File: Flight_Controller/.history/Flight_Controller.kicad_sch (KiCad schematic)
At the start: 0 parts

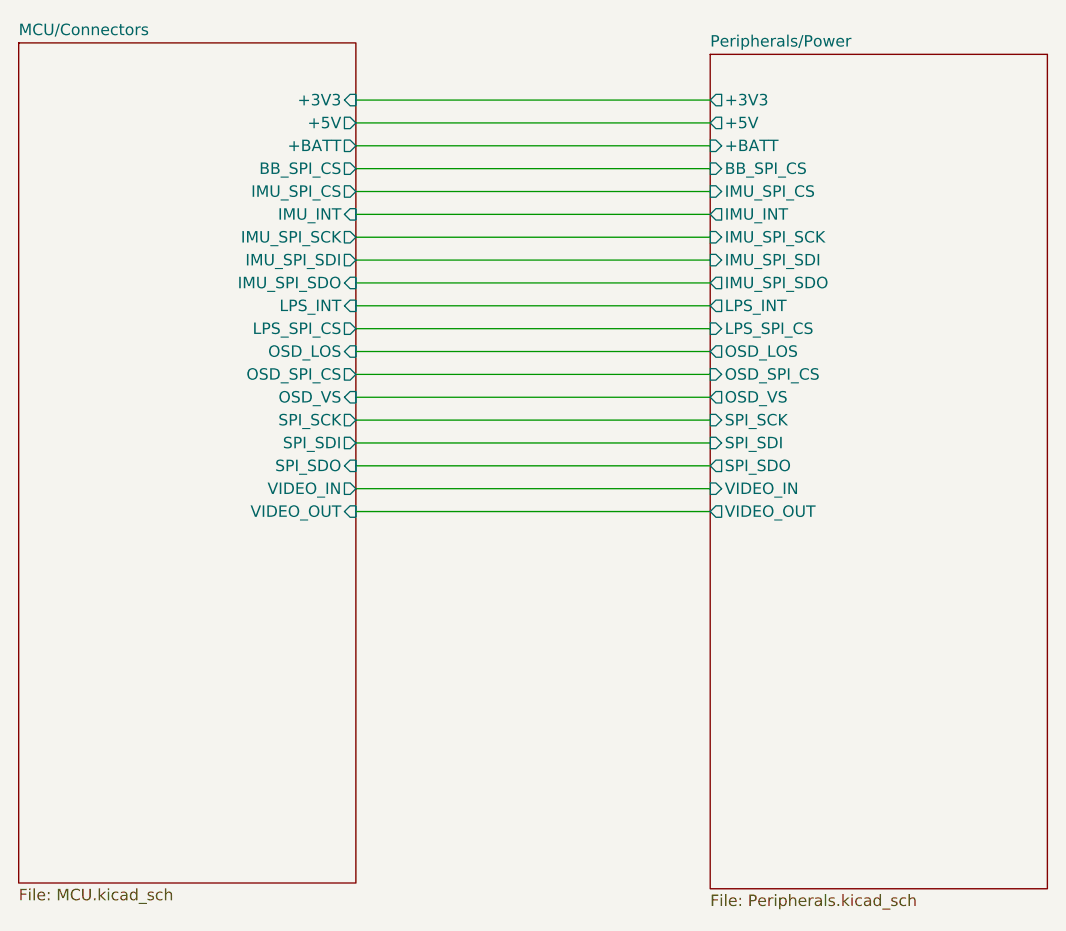
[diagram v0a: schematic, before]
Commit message: Connected all new parts to MCU, added support for hexcopter
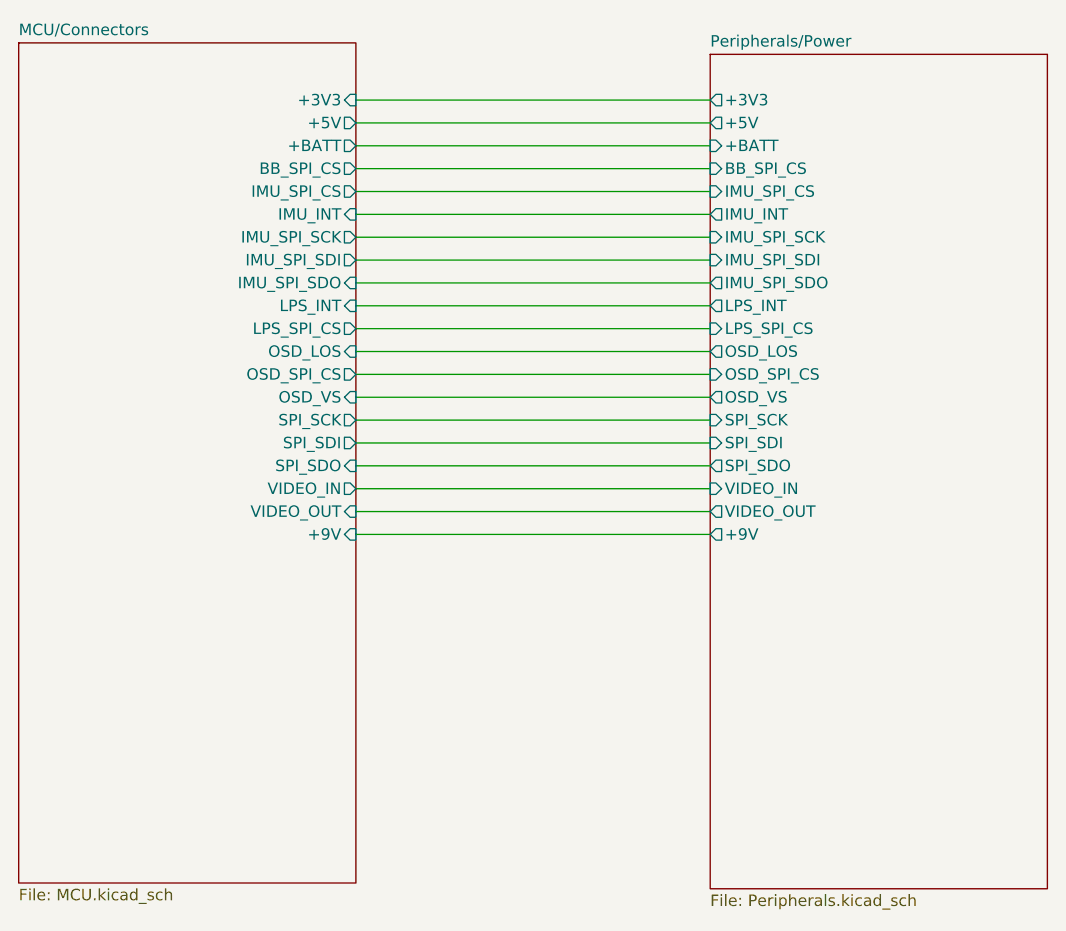
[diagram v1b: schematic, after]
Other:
- sheet MCU/Connectors ports: added +9V; removed none
- sheet Peripherals/Power ports: added +9V; removed none
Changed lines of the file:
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@@
 	(wire
 		(pts
+			(xy 54.61 153.67) (xy 93.98 153.67)
+		)
+		(stroke
+			(width 0)
+			(type default)
+		)
+	)
+	(wire
+		(pts
 			(xy 54.61 143.51) (xy 93.98 143.51)
 		)
@@
 			)
 		)
+		(pin "+9V" input
+			(at 54.61 153.67 0)
+			(effects
+				(font
+					(size 1.27 1.27)
+				)
+				(justify right)
+			)
+		)
 		(instances
 			(project "Flight_Controller"
@@
 			(effects
 				(font
+					(size 1.27 1.27)
+				)
+				(justify left)
+			)
+		)
+		(pin "+9V" output
+			(at 93.98 153.67 180)
+			(effects
+				(font

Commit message: Routing Done!
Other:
- sheet MCU/Connectors ports: added I2C_SCL1, I2C_SDA1, OSD_SPI_SCK, OSD_SPI_SDI, OSD_SPI_SDO; removed LPS_SPI_CS, OSD_LOS, OSD_VS
- sheet Peripherals/Power ports: added I2C_SCL1, I2C_SDA1, OSD_SPI_SCK, OSD_SPI_SDI, OSD_SPI_SDO; removed LPS_SPI_CS, OSD_LOS, OSD_VS
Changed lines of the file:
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@@
 	(wire
 		(pts
-			(xy 54.61 120.65) (xy 93.98 120.65)
+			(xy 54.61 153.67) (xy 93.98 153.67)
 		)
 		(stroke
@@
 	(wire
 		(pts
-			(xy 54.61 151.13) (xy 93.98 151.13)
+			(xy 54.61 120.65) (xy 93.98 120.65)
 		)
 		(stroke
@@
 	(wire
 		(pts
-			(xy 54.61 146.05) (xy 93.98 146.05)
+			(xy 54.61 143.51) (xy 93.98 143.51)
 		)
 		(stroke
@@
 	(wire
 		(pts
-			(xy 54.61 130.81) (xy 93.98 130.81)
+			(xy 54.61 138.43) (xy 93.98 138.43)
 		)
 		(stroke
@@
 	(wire
 		(pts
-			(xy 54.61 138.43) (xy 93.98 138.43)
+			(xy 54.61 140.97) (xy 93.98 140.97)
 		)
 		(stroke
@@
 	(wire
 		(pts
-			(xy 54.61 153.67) (xy 93.98 153.67)
+			(xy 54.61 146.05) (xy 93.98 146.05)
 		)
 		(stroke
@@
 	(wire
 		(pts
-			(xy 54.61 143.51) (xy 93.98 143.51)
+			(xy 54.61 135.89) (xy 93.98 135.89)
 		)
 		(stroke
@@
 	(wire
 		(pts
+			(xy 54.61 156.21) (xy 93.98 156.21)
+		)
+		(stroke
+			(width 0)
+			(type default)
+		)
+	)
+	(wire
+		(pts
 			(xy 54.61 133.35) (xy 93.98 133.35)
 		)
@@
 	(wire
 		(pts
-			(xy 54.61 140.97) (xy 93.98 140.97)
+			(xy 54.61 158.75) (xy 93.98 158.75)
 		)
 		(stroke
@@
 	(wire
 		(pts
+			(xy 54.61 151.13) (xy 93.98 151.13)
+		)
+		(stroke
+			(width 0)
+			(type default)
+		)
+	)
+	(wire
+		(pts
 			(xy 54.61 123.19) (xy 93.98 123.19)
 		)
@@
 	(wire
 		(pts
-			(xy 54.61 135.89) (xy 93.98 135.89)
+			(xy 54.61 130.81) (xy 93.98 130.81)
 		)
 		(stroke
@@
 			)
 		)
-		(pin "LPS_SPI_CS" output
+		(pin "OSD_SPI_CS" output
 			(at 54.61 130.81 0)
 			(effects
@@
 			)
 		)
-		(pin "OSD_LOS" input
+		(pin "SPI_SCK" output
 			(at 54.61 133.35 0)
 			(effects
@@
 			)
 		)
-		(pin "OSD_SPI_CS" output
+		(pin "SPI_SDI" output
 			(at 54.61 135.89 0)
 			(effects
@@
 			)
 		)
-		(pin "OSD_VS" input
+		(pin "SPI_SDO" input
 			(at 54.61 138.43 0)
 			(effects
@@
 			)
 		)
-		(pin "SPI_SCK" output
+		(pin "VIDEO_IN" output
 			(at 54.61 140.97 0)
 			(effects
@@
 			)
 		)
-		(pin "SPI_SDI" output
+		(pin "VIDEO_OUT" input
 			(at 54.61 143.51 0)
 			(effects
@@
 			)
 		)
-		(pin "SPI_SDO" input
+		(pin "+9V" input
 			(at 54.61 146.05 0)
 			(effects
@@
 			)
 		)
-		(pin "VIDEO_IN" output
+		(pin "I2C_SCL1" output
 			(at 54.61 148.59 0)
 			(effects
@@
 			)
 		)
-		(pin "VIDEO_OUT" input
+		(pin "I2C_SDA1" bidirectional
 			(at 54.61 151.13 0)
 			(effects
@@
 			)
 		)
-		(pin "+9V" input
+		(pin "OSD_SPI_SCK" output
 			(at 54.61 153.67 0)
 			(effects
@@
 			)
 		)
+		(pin "OSD_SPI_SDI" output
+			(at 54.61 156.21 0)
+			(effects
+				(font
+					(size 1.27 1.27)
+				)
+				(justify right)
+			)
+		)
+		(pin "OSD_SPI_SDO" input
+			(at 54.61 158.75 0)
+			(effects
+				(font
+					(size 1.27 1.27)
+				)
+				(justify right)
+			)
+		)
 		(instances
 			(project "Flight_Controller"
@@
 			)
 		)
-		(pin "LPS_SPI_CS" input
+		(pin "OSD_SPI_CS" input
 			(at 93.98 130.81 180)
 			(effects
@@
 			)
 		)
-		(pin "OSD_LOS" output
+		(pin "SPI_SCK" input
 			(at 93.98 133.35 180)
 			(effects
@@
 			)
 		)
-		(pin "OSD_SPI_CS" input
+		(pin "SPI_SDI" input
 			(at 93.98 135.89 180)
 			(effects
@@
 			)
 		)
-		(pin "OSD_VS" output
+		(pin "SPI_SDO" output
 			(at 93.98 138.43 180)
 			(effects
@@
 			)
 		)
-		(pin "SPI_SCK" input
+		(pin "VIDEO_IN" input
 			(at 93.98 140.97 180)
 			(effects
@@
 			)
 		)
-		(pin "SPI_SDI" input
+		(pin "VIDEO_OUT" output
 			(at 93.98 143.51 180)
 			(effects
@@
 			)
 		)
-		(pin "SPI_SDO" output
+		(pin "+9V" output
 			(at 93.98 146.05 180)
 			(effects
@@
 			)
 		)
-		(pin "VIDEO_IN" input
+		(pin "I2C_SCL1" input
 			(at 93.98 148.59 180)
 			(effects
@@
 			)
 		)
-		(pin "VIDEO_OUT" output
+		(pin "I2C_SDA1" bidirectional
 			(at 93.98 151.13 180)
 			(effects
@@
 			)
 		)
-		(pin "+9V" output
+		(pin "OSD_SPI_SCK" input
 			(at 93.98 153.67 180)
 			(effects
 				(font
+					(size 1.27 1.27)
+				)
+				(justify left)
+			)
+		)
+		(pin "OSD_SPI_SDI" input
+			(at 93.98 156.21 180)
+			(effects
+				(font
+					(size 1.27 1.27)
+				)
+				(justify left)
+			)
+		)
+		(pin "OSD_SPI_SDO" output
+			(at 93.98 158.75 180)
+			(effects
+				(font
